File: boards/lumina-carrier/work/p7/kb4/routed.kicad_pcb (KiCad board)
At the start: 4 copper layers, 100 x 80 mm, 116 parts, among them J1 LPJG0926HENL PoE+ RJ45 magjack, J2 1x6 2.54mm header (recovery), J3 DS1021-2x7SF11-B 2x7 male hea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, J4 DS1021-2x12SF11-B 2x12 male h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, SW1 SMD tactile switch, U1 TPS2378DDAR, U10 W5500, U20 SCT2A25STER, U21 TPS563201DDCR, U22 TPS16630PWPR, U30 ESP32-S3-WROOM-1-N8, Y10 25MHz 18pF CL crystal

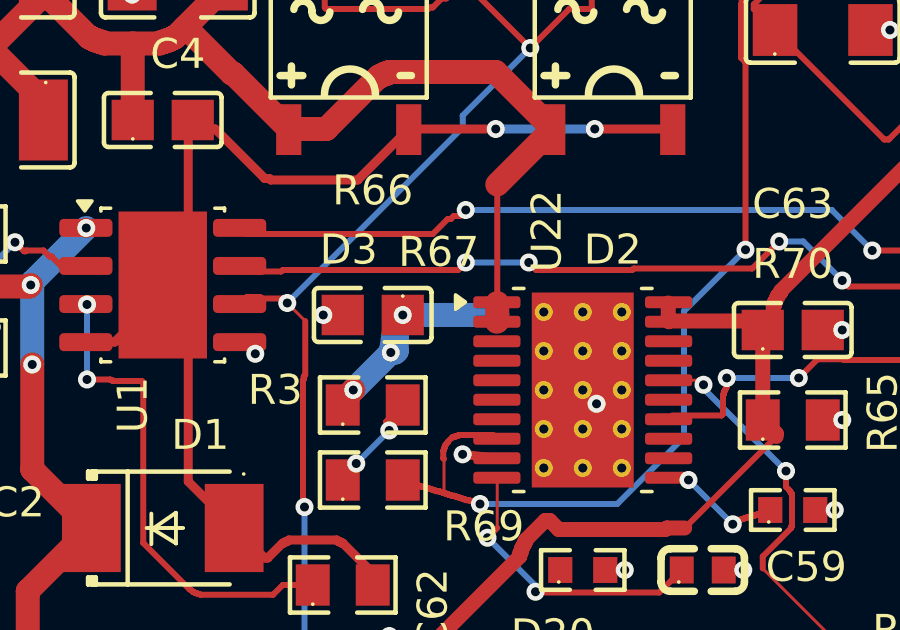
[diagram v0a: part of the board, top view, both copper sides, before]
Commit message: ai-ee lumina-carrier: backward edge - C34 moved, MDI channel 1.31 -> 2.81mm; tap nets added to voltages
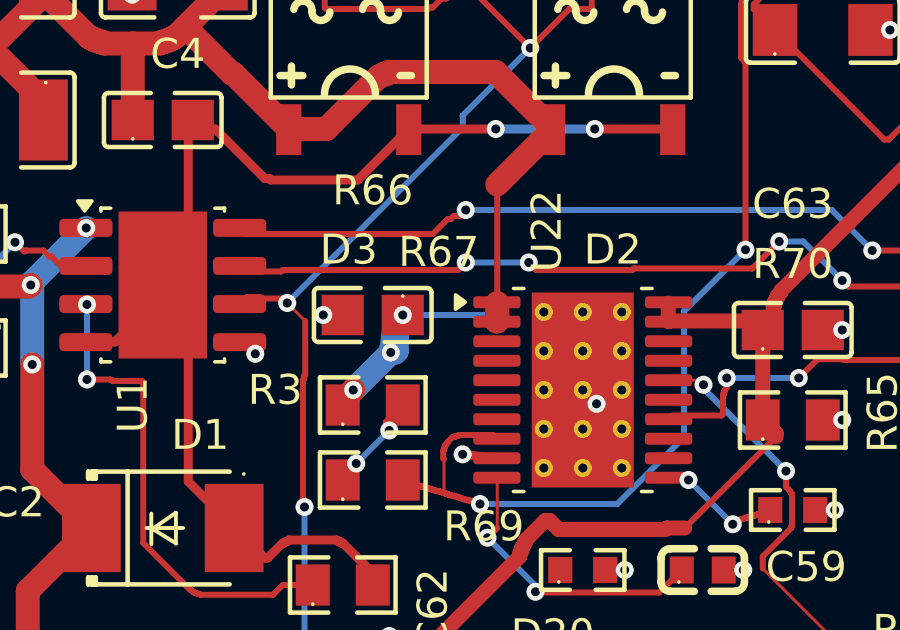
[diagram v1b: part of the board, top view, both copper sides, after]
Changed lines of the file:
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@@
 	)
 	(segment
-		(start 41.15 93.5)
-		(end 38 93.5)
-		(width 0.8)
-		(layer "B.Cu")
-		(net "V48_RAW")
-	)
-	(segment
 		(start 41.15 93.481818)
 		(end 41.15 93.5)
@@
 	(segment
 		(start 41.150000 93.500000)
+		(end 38.000000 93.500000)
+		(width 0.2)
+		(layer "B.Cu")
+		(net "V48_RAW")
+	)
+	(segment
+		(start 41.150000 93.500000)
